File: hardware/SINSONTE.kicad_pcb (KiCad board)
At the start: 2 copper layers, 90 x 70 mm, 35 parts, among them J1 BAT, J10 Conn_01x01_Male, J11 Conn_01x01_Male, J12 Conn_01x04_Male, J13 Conn_01x01_Male, J14 Conn_01x02_Male, J2 CLOCK, J3 LIGHT_SENSOR, J4 Conn_01x17_Male, J5 Conn_01x01_Male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

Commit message: some pcb decorations
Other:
- board text added: "SINSONTE"
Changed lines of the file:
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@@
   (general
     (thickness 1.6)
-    (drawings 6)
+    (drawings 10)
     (tracks 205)
     (zones 0)
@@
     (descr "2xAA cell battery holder, Keystone P/N 2462, https://www.keyelco.com/product-pdf.cfm?p=1027")
     (tags "AA battery cell holder")
-    (fp_text reference BT1 (at -5.08 -6.35 180) (layer F.SilkS)
+    (fp_text reference BT1 (at -4.755 17.78 180) (layer F.SilkS)
       (effects (font (size 1 1) (thickness 0.15)))
     )
@@
       (net 28 "Net-(J4-Pad1)"))
   )
-  (gr_circle (center 125 66) (end 139 66) (layer F.SilkS) (width 0.12))
+  (gr_text SINSONTE (at 120.015 89.535 90) (layer F.SilkS)
+    (effects (font (size 2 2) (thickness 0.35)))
+  )
+  (gr_line (start 135.2 76.2) (end 140 81) (layer F.SilkS) (width 1.5))
+  (gr_line (start 140 120) (end 140 81) (layer F.SilkS) (width 1.5))
+  (gr_line (start 50 120) (end 140 120) (layer F.SilkS) (width 1.5))
+  (gr_circle (center 125 66) (end 139 66) (layer F.SilkS) (width 0.5))
   (gr_circle (center 125 66) (end 133 66) (layer Edge.Cuts) (width 0.05))
   (gr_line (start 140 50) (end 140 120) (layer Edge.Cuts) (width 0.05))

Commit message: top silks finished
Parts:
- added G***: LOGO, Logos_Galopago:sinsonte_logo_11x6mm, F.Cu at (53.5, 89.5)

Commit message: all silks finished
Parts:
- added G***: LOGO, Logos_Galopago:sinsonte_logo_11x6mm_cu, B.Cu at (68.6, 113.7)
- added G***: LOGO, Logos_Galopago:sinsonte_logo_11x6mm, B.Cu at (114.9, 80.6)
- added REF**: OSHW-Symbol_8.9x8mm_Copper, Symbol:OSHW-Symbol_8.9x8mm_Copper, B.Cu at (108.6, 113.0)

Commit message: gerbers generated
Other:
- board text added: "- +"
- board text added: "1 2 3"
- board text added: "V1"
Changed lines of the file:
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@@
   (general
     (thickness 1.6)
-    (drawings 19)
+    (drawings 22)
     (tracks 205)
     (zones 0)
@@
     (visible_elements FFFFFF7F)
     (pcbplotparams
-      (layerselection 0x00000_fffffffe)
+      (layerselection 0x010f0_ffffffff)
       (usegerberextensions false)
       (usegerberattributes false)
@@
       (padsonsilk false)
       (subtractmaskfromsilk false)
-      (outputformat 5)
+      (outputformat 1)
       (mirror false)
-      (drillshape 1)
+      (drillshape 0)
       (scaleselection 1)
       (outputdirectory "gerber/"))
@@
       (net 28 "Net-(J4-Pad1)"))
   )
+  (gr_text V1 (at 132.08 116.84) (layer B.SilkS)
+    (effects (font (size 1 1) (thickness 0.15)) (justify mirror))
+  )
+  (gr_text "1  2  3" (at 131.445 102.87) (layer F.SilkS)
+    (effects (font (size 1 1) (thickness 0.15)))
+  )
+  (gr_text "-  +" (at 112.395 55.245) (layer F.SilkS)
+    (effects (font (size 1 1) (thickness 0.15)))
+  )
   (gr_text SINSONTE (at 88.265 114.3) (layer B.SilkS)

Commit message: cu plane added front
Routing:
- added copper zone on F.Cu, net Net-(BT1-Pad2)
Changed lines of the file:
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@@
+    )
+  )
+  (zone (net 4) (net_name "Net-(BT1-Pad2)") (layer F.Cu) (hatch edge 0.508)
+    (connect_pads (clearance 0.508))
+    (min_thickness 0.254)
+    (fill yes (arc_segments 32) (thermal_gap 0.508) (thermal_bridge_width 0.508))
+    (polygon
+      (pts
+        (xy 146.685 123.825) (xy 45.72 123.825) (xy 45.72 41.275) (xy 146.685 41.275)
+      )
     )
   )

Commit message: capacitor fixed polarity
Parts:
- C1: value CP -> 10uF
- C2: value C -> 0.1uF
- C4: value CP -> 100uF
- R1: value R -> 100k
- R2: value R -> 100
- R3: value R -> 10
- R4: value R -> 220
- R6: value R -> 2.2k
- moved C4 2.69 mm to (99.3, 53.6), turned to 0 degrees
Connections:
- C4 pad 1: Net-(C4-Pad1) -> Net-(C2-Pad1)
- C4 pad 2: Net-(C2-Pad1) -> Net-(C4-Pad2)
- Q2 pad 2: Net-(C4-Pad1) -> Net-(C4-Pad2)
- R6 pad 2: Net-(C4-Pad1) -> Net-(C4-Pad2)
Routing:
- net Net-(C4-Pad2): track 0.00 -> 8.05 mm
- net Net-(C4-Pad1): track 7.86 -> 0.00 mm

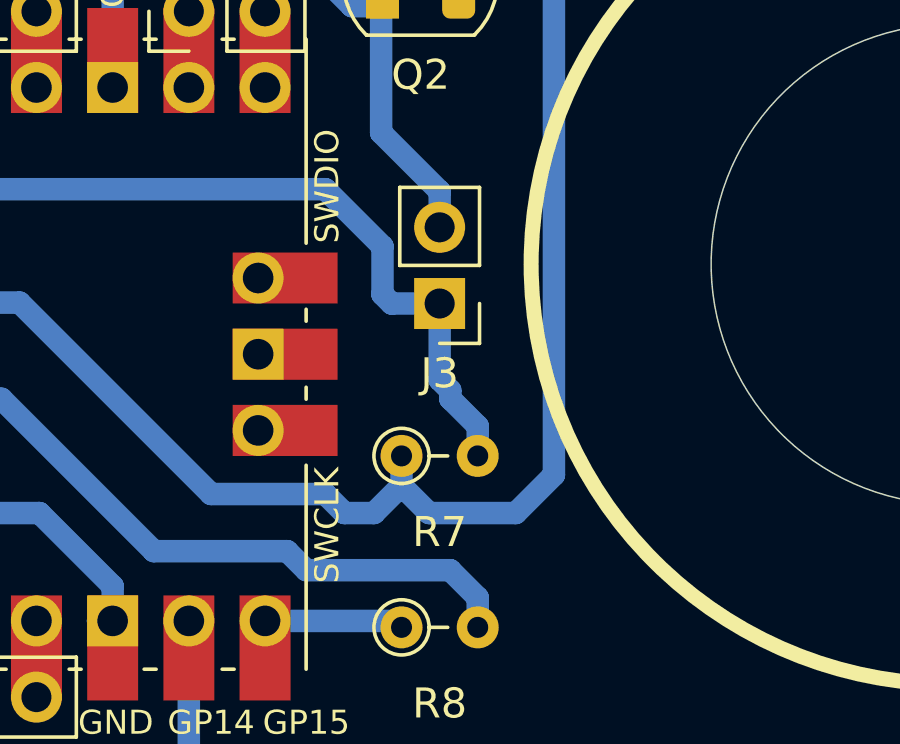
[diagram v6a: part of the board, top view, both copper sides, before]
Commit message: changed light sensor resistor to pull-down
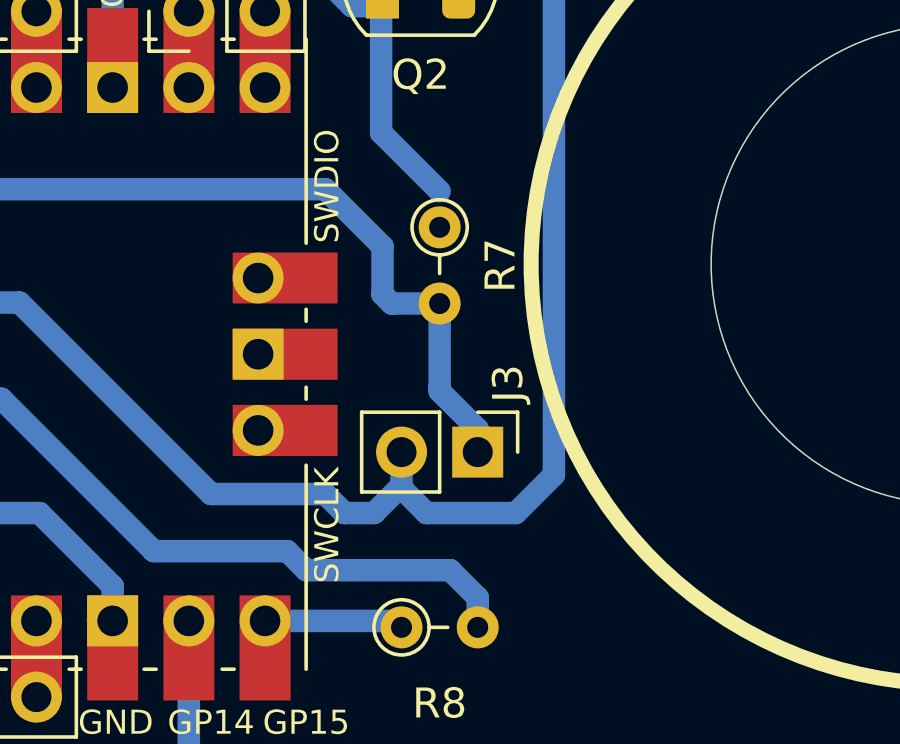
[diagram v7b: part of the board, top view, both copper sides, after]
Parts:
- moved R7 7.73 mm to (108.0, 64.8), turned to 270 degrees
- moved J3 5.11 mm to (109.2, 72.3), turned to 270 degrees
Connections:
- J3 pad 2: Net-(BT1-Pad2) -> Net-(J3-Pad2)
- J6 pad 1: Net-(J6-Pad1) -> Net-(J3-Pad2)
- JP1 pad 1: Net-(J6-Pad1) -> Net-(J3-Pad2)
- LS1 pad 1: Net-(J6-Pad1) -> Net-(J3-Pad2)
- R7 pad 1: Net-(J6-Pad1) -> Net-(BT1-Pad2)
- U1 pad 36: Net-(J6-Pad1) -> Net-(J3-Pad2)
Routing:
- net Net-(J3-Pad2): track 0.00 -> 82.2 mm
- net Net-(J6-Pad1): track 82.1 -> 0.00 mm
- net Net-(BT1-Pad2): track 322.9 -> 321.7 mm
